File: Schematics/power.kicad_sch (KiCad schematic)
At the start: 0 parts

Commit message: Power + Servo
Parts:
- added BT? (x2): AA, symbol Device:Battery
- added C?: 10uF, symbol Device:C_Small
- added L?: 4.7uH, symbol Device:L_Small
- added U?: XC9142B50CMR-G, SC_50CMR-G_TOR, symbol SFRLibraries:XC9142B50CMR-G
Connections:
- new net: L?.2, U?.5 (LX)
- new net +5V: U?.4 (VOUT)
- new net Earth: BT?.2 (-), BT?.2 (-), C?.2, U?.2 (GND)
- new net MotorEnable: U?.1 (CE)
- new net VCC: BT?.1 (+), BT?.1 (+), C?.1, L?.1

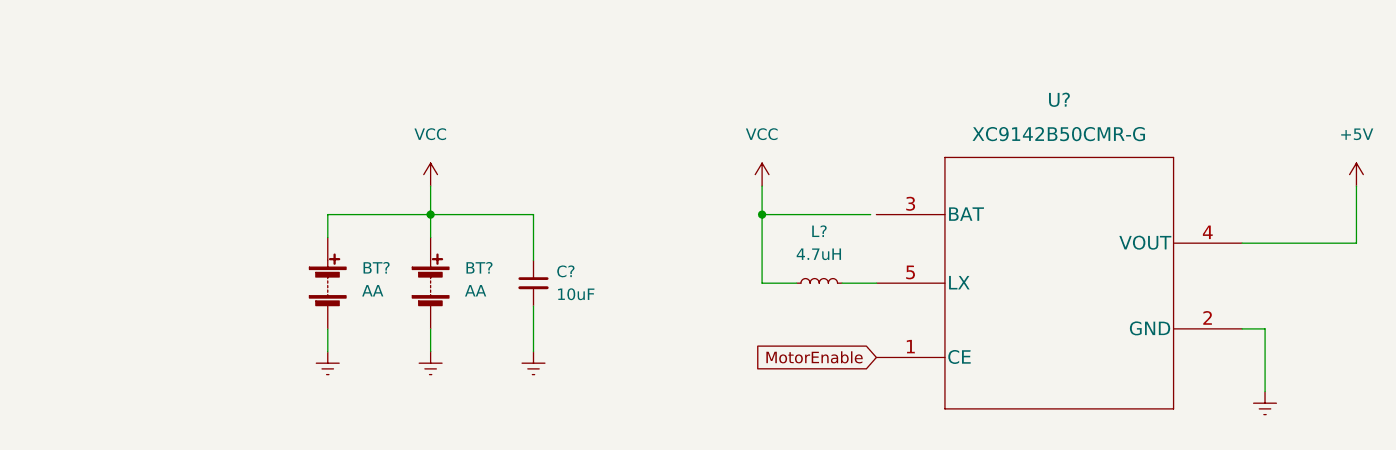
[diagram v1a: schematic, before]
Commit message: Changed MCU
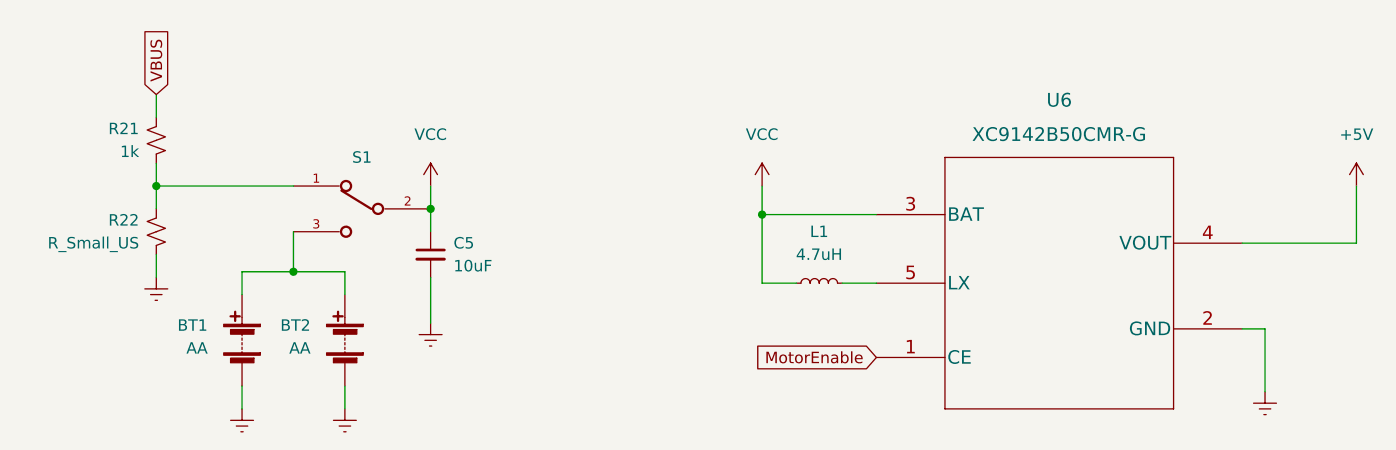
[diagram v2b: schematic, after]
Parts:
- removed BT? (x2): AA, symbol Device:Battery
- removed C?: 10uF, symbol Device:C_Small
- added BT1, BT2: AA, symbol Device:Battery
- added C5: 10uF, symbol Device:C_Small
- added R21: 1k, symbol Device:R_Small_US
- added R22: R_Small_US, symbol Device:R_Small_US
- added S1: a, SW_JS102011SAQN, symbol SFRLibraries:JS102011SAQN
- gave numbers to parts that had none: 2
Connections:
- net Earth: now also BT1.2 (-), BT2.2 (-), C5.2, R22.2
- net VCC: now also U6.3 (BAT), C5.1, S1.2
- new net: BT1.1 (+), BT2.1 (+), S1.3
- new net: R21.2, R22.1, S1.1
- new net VBUS: R21.1

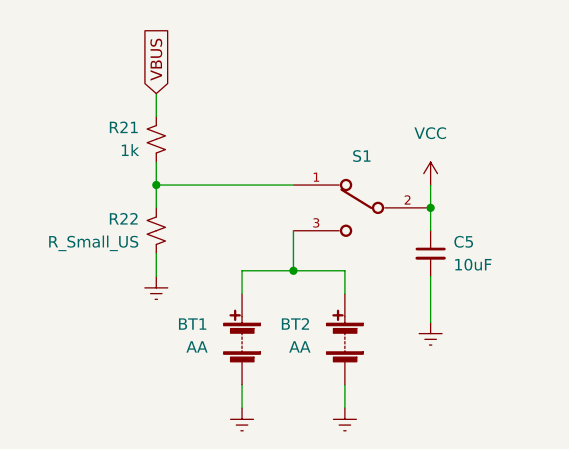
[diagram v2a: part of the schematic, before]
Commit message: Added Footprints
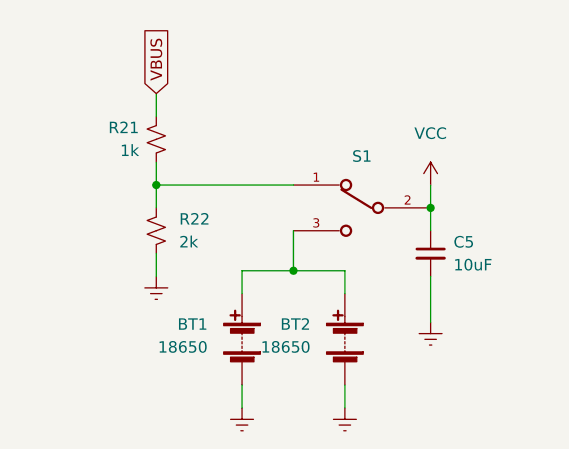
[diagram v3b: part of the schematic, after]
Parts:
- BT1, BT2: value AA -> 18650; footprint (none) -> SFRFootprints:1049P
- C5, R21: footprint (none) -> Resistor_SMD:R_0603_1608Metric_Pad0.98x0.95mm_HandSolder
- L1: footprint (none) -> Inductor_SMD:L_0603_1608Metric_Pad1.05x0.95mm_HandSolder
- R22: value R_Small_US -> 2k; footprint (none) -> Resistor_SMD:R_0603_1608Metric_Pad0.98x0.95mm_HandSolder
- U6: footprint SC_50CMR-G_TOR -> SFRFootprints:XC9142B50CMR-G
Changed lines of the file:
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@@
       (effects (font (size 1.27 1.27)) (justify left))
     )
-    (property "Value" "AA" (id 1) (at 83.185 108.8389 0)
-      (effects (font (size 1.27 1.27)) (justify left))
-    )
-    (property "Footprint" "" (id 2) (at 86.995 106.426 90)
+    (property "Value" "18650" (id 1) (at 83.185 108.8389 0)
+      (effects (font (size 1.27 1.27)) (justify left))
+    )
+    (property "Footprint" "SFRFootprints:1049P" (id 2) (at 86.995 106.426 90)
       (effects (font (size 1.27 1.27)) hide)
     )
@@
       (effects (font (size 1.27 1.27)) (justify left))
     )
-    (property "Value" "AA" (id 1) (at 94.615 108.8389 0)
-      (effects (font (size 1.27 1.27)) (justify left))
-    )
-    (property "Footprint" "" (id 2) (at 98.425 106.426 90)
+    (property "Value" "18650" (id 1) (at 94.615 108.8389 0)
+      (effects (font (size 1.27 1.27)) (justify left))
+    )
+    (property "Footprint" "SFRFootprints:1049P" (id 2) (at 98.425 106.426 90)
       (effects (font (size 1.27 1.27)) hide)
     )
@@
       (effects (font (size 1.524 1.524)))
     )
-    (property "Footprint" "SC_50CMR-G_TOR" (id 2) (at 177.8 86.614 0)
+    (property "Footprint" "SFRFootprints:XC9142B50CMR-G" (id 2) (at 177.8 86.614 0)
       (effects (font (size 1.524 1.524)) hide)
     )
@@
     (property "Reference" "L1" (id 0) (at 151.13 95.885 90))
     (property "Value" "4.7uH" (id 1) (at 151.13 98.425 90))
-    (property "Footprint" "" (id 2) (at 151.13 101.6 0)
+    (property "Footprint" "Inductor_SMD:L_0603_1608Metric_Pad1.05x0.95mm_HandSolder" (id 2) (at 151.13 101.6 0)
       (effects (font (size 1.27 1.27)) hide)
     )
@@
   (symbol (lib_id "Device:R_Small_US") (at 77.47 95.885 0) (mirror y) (unit 1)
     (in_bom yes) (on_board yes) (fields_autoplaced)
-    (property "Reference" "R22" (id 0) (at 75.565 94.6149 0)
-      (effects (font (size 1.27 1.27)) (justify left))
-    )
-    (property "Value" "R_Small_US" (id 1) (at 75.565 97.1549 0)
-      (effects (font (size 1.27 1.27)) (justify left))
-    )
-    (property "Footprint" "" (id 2) (at 77.47 95.885 0)
+    (property "Reference" "R22" (id 0) (at 80.01 94.6149 0)
+      (effects (font (size 1.27 1.27)) (justify right))
+    )
+    (property "Value" "2k" (id 1) (at 80.01 97.1549 0)
+      (effects (font (size 1.27 1.27)) (justify right))
+    )
+    (property "Footprint" "Resistor_SMD:R_0603_1608Metric_Pad0.98x0.95mm_HandSolder" (id 2) (at 77.47 95.885 0)
       (effects (font (size 1.27 1.27)) hide)
     )
@@
       (effects (font (size 1.27 1.27)) (justify left))
     )
-    (property "Footprint" "" (id 2) (at 107.95 98.425 0)
+    (property "Footprint" "Resistor_SMD:R_0603_1608Metric_Pad0.98x0.95mm_HandSolder" (id 2) (at 107.95 98.425 0)
       (effects (font (size 1.27 1.27)) hide)
     )
@@
       (effects (font (size 1.27 1.27)) (justify left))
     )
-    (property "Footprint" "" (id 2) (at 77.47 85.725 0)
-      (effects (font (size 1.27 1.27)) hide)
-    )
+    (property "Footprint" "Resistor_SMD:R_0603_1608Metric_Pad0.98x0.95mm_HandSolder" (id 2) (at 77.47 85.725 0)
+      (effects (font (size 1.27 1.27)) hide)
+    )

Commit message: PCB
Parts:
- S1: footprint SW_JS102011SAQN -> SFRFootprints:SW_JS102011SAQN
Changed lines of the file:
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@@
       (effects (font (size 1.27 1.27)) hide)
     )
-    (property "Footprint" "SW_JS102011SAQN" (id 2) (at 100.33 93.345 0)
+    (property "Footprint" "SFRFootprints:SW_JS102011SAQN" (id 2) (at 100.33 93.345 0)
       (effects (font (size 1.27 1.27)) (justify left bottom) hide)
     )
